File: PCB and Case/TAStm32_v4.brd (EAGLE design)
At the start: 100 x 50 mm, 55 parts, among them CN1 330pF, CN2 330pF, CN3 330pF, CN4 330pF, IC1 74HCT3G07DP-Q100H, IC2 74HCT3G07DP-Q100H, IC3 74AVCH4T245PW,118, IC4 74AVCH4T245PW,118, J1 ZX62D-B-5PA8, J10 RJSSE538002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

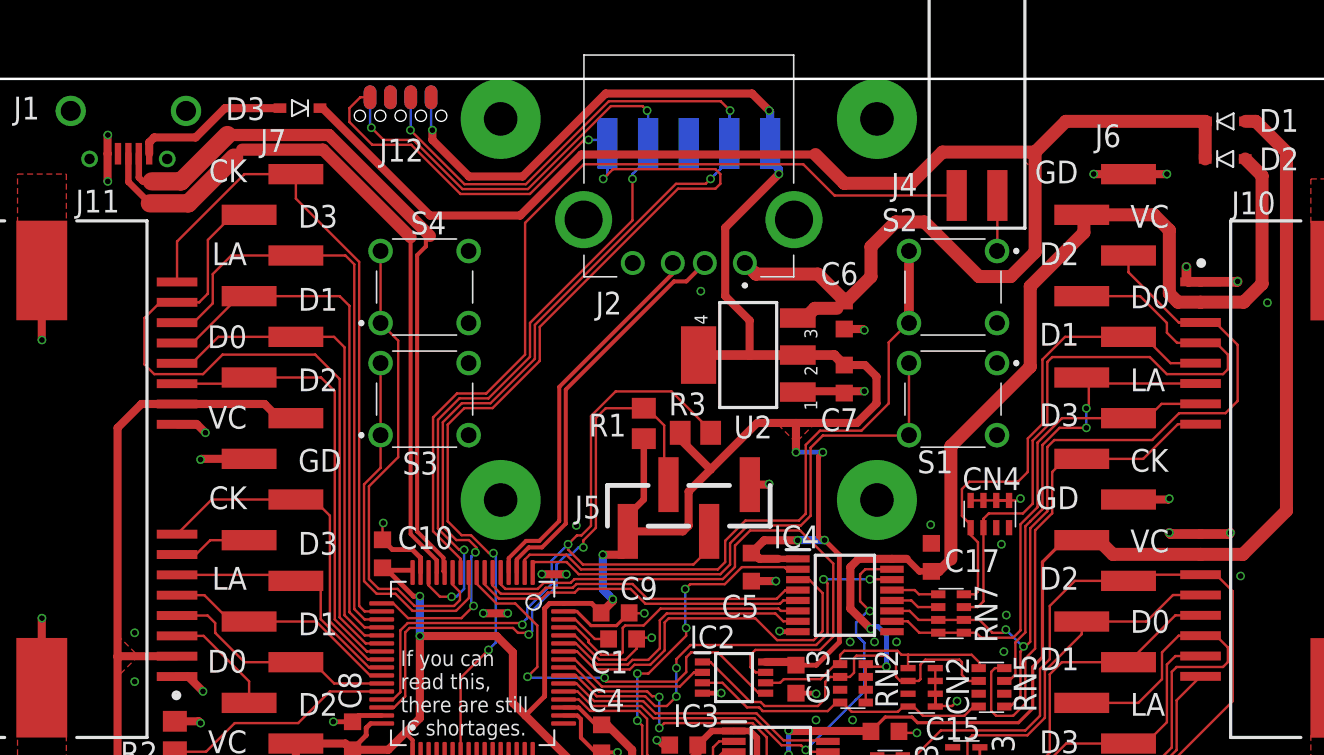
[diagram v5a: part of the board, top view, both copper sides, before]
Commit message: rerouted vis board, rev2 cleanups
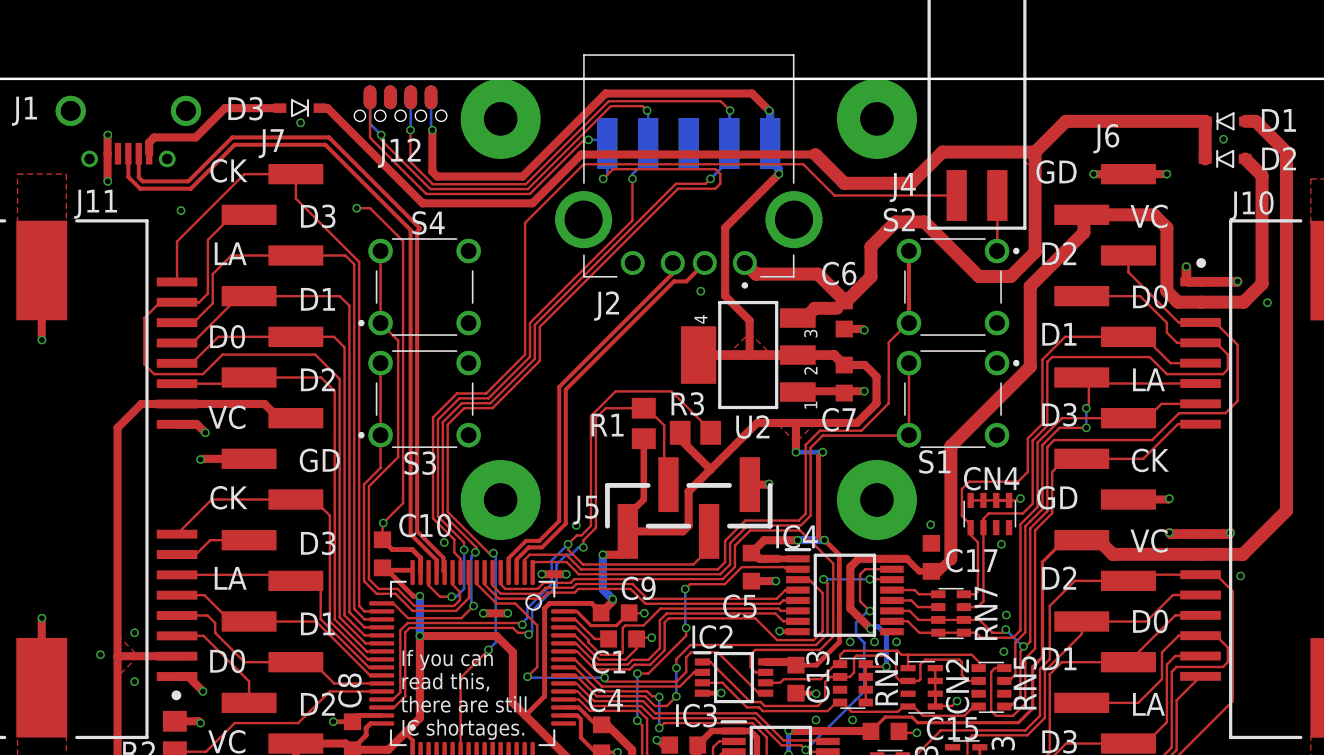
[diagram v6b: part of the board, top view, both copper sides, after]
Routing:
- net GND: track 136.8 -> 158.6 mm, vias 69 -> 75
- net NRST: track 80.3 -> 78.3 mm
- net V+: track 276.4 -> 277.6 mm
- net DM: track 45.6 -> 44.9 mm
- net SWCLK: track 74.3 -> 75.0 mm
- net +5V: track 98.3 -> 97.7 mm

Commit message: more board tidyups
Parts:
- C15, C17: value 100nF -> 4.7uF
- S1, S2, S3, S4: value SWITCHN -> 3-1825910-1_SWITCHN; device 3-1825910-1:318259101 -> TAStm32_v4:3-1825910-1_318259101
- moved R1 1.37 mm to (45.8, 28.5)
- moved R3 0.89 mm to (49.7, 28.4)
- moved S1 0.50 mm to (66.0, 30.0)
- moved S2 0.50 mm to (66.0, 37.0)
- moved S3 0.50 mm to (34.0, 30.0), turned to 0 degrees
- moved S4 0.50 mm to (34.0, 37.0), turned to 0 degrees
- moved C1 0.22 mm to (46.0, 14.9)
- moved R2 0.15 mm to (17.9, 9.08)
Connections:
- net GND: now also S1.3, S1.4, S2.3, S2.4; no longer S1.1, S1.2, S2.1, S2.2
- net SWITCH1: now also S1.1, S1.2; no longer S1.3, S1.4
- net SWITCH2: now also S2.1, S2.2; no longer S2.3, S2.4
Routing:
- net SWITCH1: track 35.8 -> 30.3 mm
- net SWITCH4: track 30.1 -> 25.6 mm
- net SWITCH3: track 23.3 -> 18.8 mm
- net SWITCH2: track 41.8 -> 38.7 mm
- net GND: track 158.6 -> 155.5 mm
- net P2_VCC: track 69.5 -> 71.6 mm
- net DM: track 44.9 -> 44.3 mm
- net I2C_SDA: track 38.2 -> 37.5 mm
- net +5V: track 97.7 -> 98.3 mm

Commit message: part number updates
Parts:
- IC1, IC2: value 74HCT3G07DP-Q100H -> 74LVC3G17DP
- IC3, IC4: value 74AVCH4T245PW,118 -> 74AXP4T245
- RN5: value 47K -> 47R
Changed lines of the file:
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@@
 <attribute name="VALUE" x="71.7272" y="0.472" size="1.27" layer="27" rot="R90"/>
 </element>
-<element name="RN5" library="resistor-net" library_urn="urn:adsk.eagle:library:343" package="CTS742C083" package3d_urn="urn:adsk.eagle:package:24985/1" value="47K" x="68.9024" y="12" smashed="yes" rot="R90">
+<element name="RN5" library="resistor-net" library_urn="urn:adsk.eagle:library:343" package="CTS742C083" package3d_urn="urn:adsk.eagle:package:24985/1" value="47R" x="68.9024" y="12" smashed="yes" rot="R90">
 <attribute name="MF" value="" x="68.9024" y="12" size="1.778" layer="27" rot="R90" display="off"/>
 <attribute name="MPN" value="" x="68.9024" y="12" size="1.778" layer="27" rot="R90" display="off"/>
@@
 <attribute name="VALUE" x="59.7728" y="8.278" size="1.27" layer="27" rot="R270"/>
 </element>
-<element name="IC1" library="SamacSys_Parts" package="SOP65P400X110-8N" value="74HCT3G07DP-Q100H" x="53.4092" y="2.25" smashed="yes" rot="R180">
+<element name="IC1" library="SamacSys_Parts" package="SOP65P400X110-8N" value="74LVC3G17DP" x="53.4092" y="2.25" smashed="yes" rot="R180">
 <attribute name="DESCRIPTION" value="74HC(T)3G07-Q100 - Triple buffer with open-drain outputs@en-us" x="53.4092" y="2.25" size="1.778" layer="27" rot="R180" display="off"/>
 <attribute name="HEIGHT" value="1.1mm" x="53.4092" y="2.25" size="1.778" layer="27" rot="R180" display="off"/>
@@
 <attribute name="VALUE" x="53.4092" y="2.25" size="1.27" layer="27" rot="R180" align="center"/>
 </element>
-<element name="IC2" library="SamacSys_Parts" package="SOP65P400X110-8N" value="74HCT3G07DP-Q100H" x="52.8236" y="12.6096" smashed="yes">
+<element name="IC2" library="SamacSys_Parts" package="SOP65P400X110-8N" value="74LVC3G17DP" x="52.8236" y="12.6096" smashed="yes">
 <attribute name="DESCRIPTION" value="74HC(T)3G07-Q100 - Triple buffer with open-drain outputs@en-us" x="52.8236" y="12.6096" size="1.778" layer="27" display="off"/>
 <attribute name="HEIGHT" value="1.1mm" x="52.8236" y="12.6096" size="1.778" layer="27" display="off"/>
@@
 <attribute name="VALUE" x="52.8236" y="12.6096" size="1.27" layer="27" align="center"/>
 </element>
-<element name="IC3" library="SamacSys_Parts" package="SOP65P640X110-16N" value="74AVCH4T245PW,118" x="55.75" y="7" smashed="yes">
+<element name="IC3" library="SamacSys_Parts" package="SOP65P640X110-16N" value="74AXP4T245" x="55.75" y="7" smashed="yes">
 <attribute name="DESCRIPTION" value="74AVCH4T245 - 4-bit dual supply translating transceiver with configurable voltage translation; 3-state@en-us" x="55.75" y="7" size="1.778" layer="27" display="off"/>
 <attribute name="HEIGHT" value="1.1mm" x="55.75" y="7" size="1.778" layer="27" display="off"/>
@@
 <attribute name="VALUE" x="63.5856" y="18.3896" size="1.27" layer="27" rot="R270"/>
 </element>
-<element name="IC4" library="SamacSys_Parts" package="SOP65P640X110-16N" value="74AVCH4T245PW,118" x="59.75" y="17.75" smashed="yes">
+<element name="IC4" library="SamacSys_Parts" package="SOP65P640X110-16N" value="74AXP4T245" x="59.75" y="17.75" smashed="yes">
 <attribute name="DESCRIPTION" value="74AVCH4T245 - 4-bit dual supply translating transceiver with configurable voltage translation; 3-state@en-us" x="54.1112" y="17.75" size="1.778" layer="27" display="off"/>
 <attribute name="HEIGHT" value="1.1mm" x="54.1112" y="17.75" size="1.778" layer="27" display="off"/>
